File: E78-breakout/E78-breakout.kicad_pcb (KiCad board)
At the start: 2 copper layers, 31.8 x 30.5 mm, 24 parts, among them J1 Conn_01x04, J2 Conn_01x06, J3 Conn_01x04, J4 Conn_01x03, U1 E78, U2 AMS1117CS-3.3

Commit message: routed e78 breakout
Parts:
- added kibuzzard-64A3B516: G***, kibuzzard-64A3B516, B.Cu at (103.5, 127.0)
- added kibuzzard-64A3B52E: G***, kibuzzard-64A3B52E, B.Cu at (106.0, 127.0)
- added kibuzzard-64A3B571: G***, kibuzzard-64A3B571, B.Cu at (101.0, 127.0)
- added kibuzzard-64A3B5A1: G***, kibuzzard-64A3B5A1, B.Cu at (116.8, 127.0)
- added kibuzzard-64A3B5B5: G***, kibuzzard-64A3B5B5, B.Cu at (114.3, 127.0)
- added kibuzzard-64A3B5D3: G***, kibuzzard-64A3B5D3, B.Cu at (119.4, 127.0)
- added kibuzzard-64A3B602: G***, kibuzzard-64A3B602, B.Cu at (121.9, 108.0)
- added kibuzzard-64A3B618: G***, kibuzzard-64A3B618, B.Cu at (122.3, 113.0)
- added kibuzzard-64A3B61D: G***, kibuzzard-64A3B61D, B.Cu at (122.3, 110.5)
- added kibuzzard-64A3B637: G***, kibuzzard-64A3B637, B.Cu at (121.9, 115.6)
- added kibuzzard-64A3B63B: G***, kibuzzard-64A3B63B, B.Cu at (122.0, 118.1)
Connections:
- U1 pad 20: Net-(J2-Pin_2) -> Net-(J2-Pin_3)
- U1 pad 21: Net-(J2-Pin_3) -> Net-(J2-Pin_2)
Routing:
- net +3V3: track 0.00 -> 74.5 mm, vias 0 -> 3
- net +3.3VA: track 0.00 -> 32.7 mm
- net Net-(J3-Pin_3): track 0.00 -> 27.0 mm
- net Net-(J3-Pin_2): track 0.00 -> 25.9 mm
- net Net-(J2-Pin_4): track 0.00 -> 24.5 mm, vias 0 -> 1
- net Net-(J2-Pin_5): track 0.00 -> 24.1 mm, vias 0 -> 1
- net Net-(J1-Pin_3): track 0.00 -> 21.6 mm
- net Net-(J1-Pin_2): track 0.00 -> 21.4 mm
- net GND: track 0.00 -> 12.6 mm, vias 0 -> 5
- net Net-(J2-Pin_3): track 0.00 -> 9.18 mm, vias 0 -> 1
- net Net-(J2-Pin_2): track 0.00 -> 8.67 mm, vias 0 -> 1
- net Net-(U1-ADC_IN): track 0.00 -> 8.62 mm, vias 0 -> 1
- net Net-(U1-BUSY): track 0.00 -> 8.59 mm, vias 0 -> 1
- net Net-(U1-SETA): track 0.00 -> 6.87 mm, vias 0 -> 1
- net Net-(U1-AUX): track 0.00 -> 6.29 mm, vias 0 -> 1
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- added copper zone on B.Cu, net +3V3
- added copper zone on B.Cu, net GND
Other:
- outline, holes or cut-outs redrawn

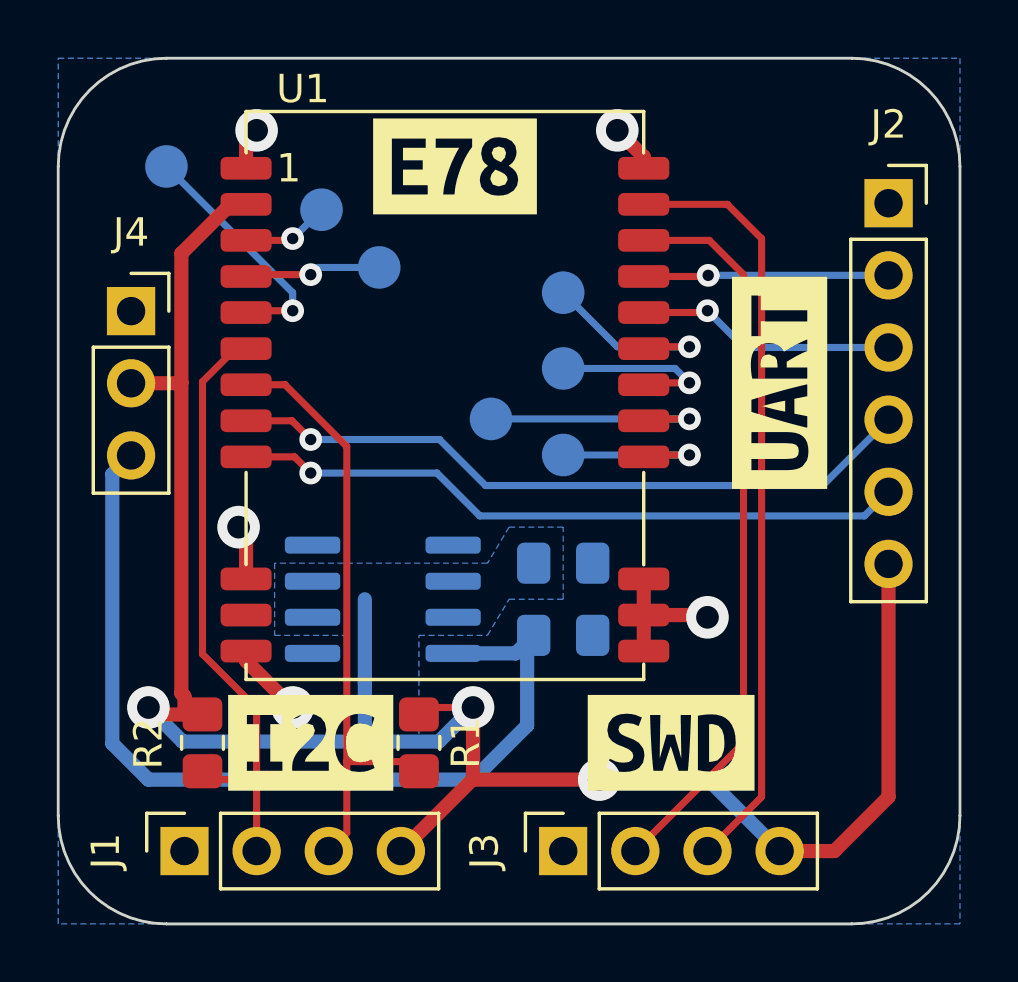
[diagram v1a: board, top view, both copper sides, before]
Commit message: version from which e78 breakout was generated
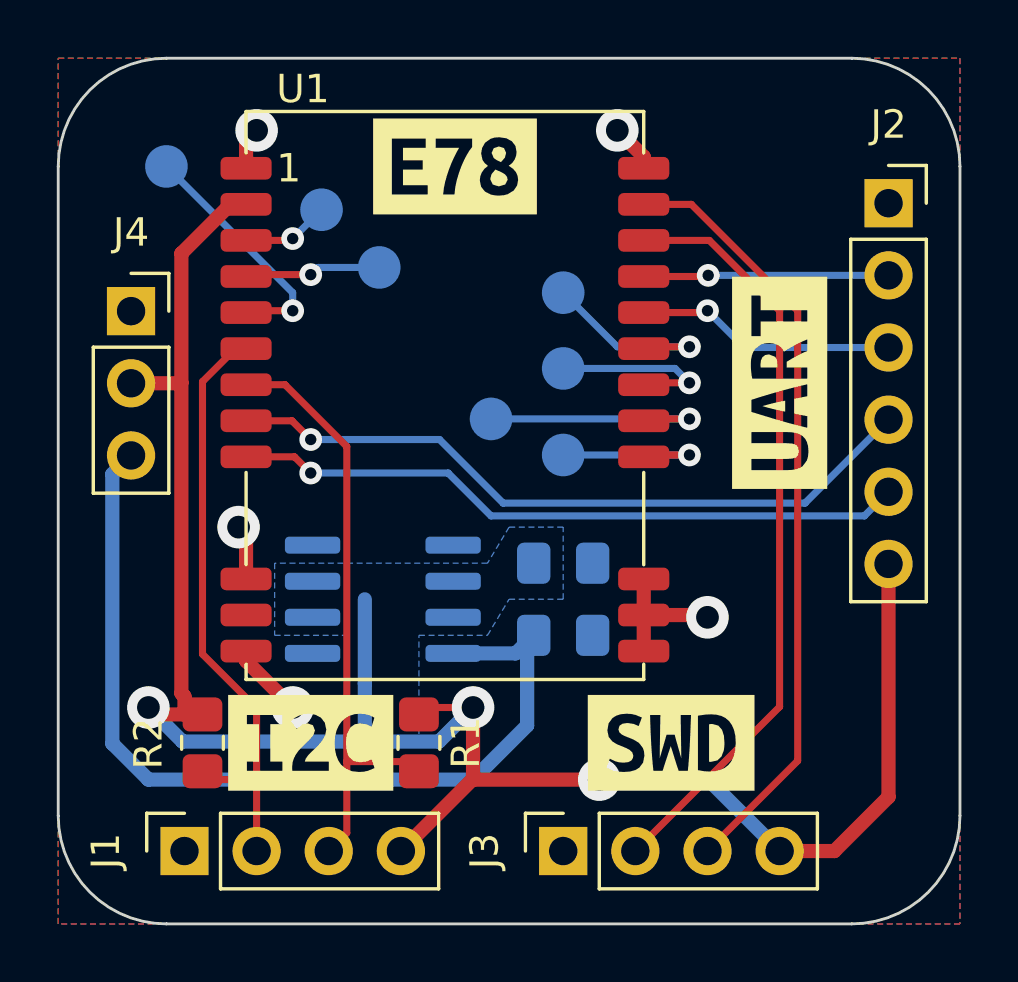
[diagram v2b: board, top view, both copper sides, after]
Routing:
- net Net-(J3-Pin_2): track 25.9 -> 26.9 mm
- net Net-(J2-Pin_4): track 24.5 -> 25.0 mm
- added copper zone on F.Cu, net +3V3
